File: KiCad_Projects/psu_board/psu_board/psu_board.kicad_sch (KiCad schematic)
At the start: 23 parts, among them J1 Conn_01x02_Female, J2 Conn_01x02_Female, J3 Conn_01x02_Female, SW1 SW_DIP_x01, SW2 SW_DIP_x01, SW3 SW_DIP_x01, SW4 SW_DIP_x01, SW5 SW_DIP_x01, U1 OKL-T_6-W12N-C

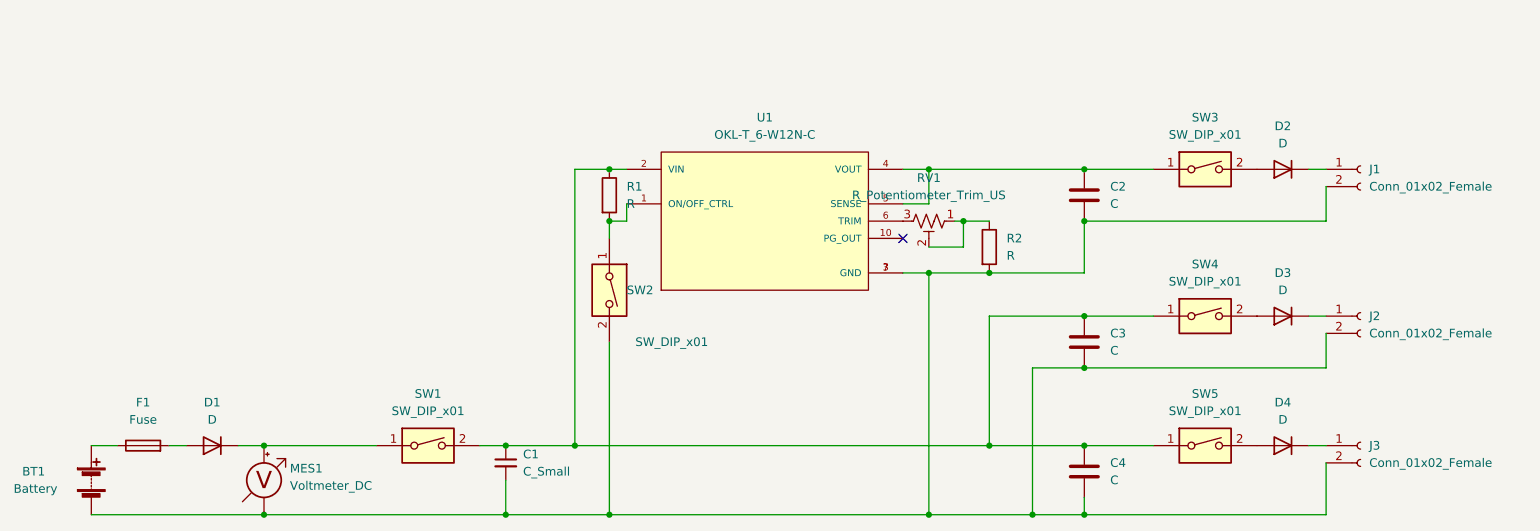
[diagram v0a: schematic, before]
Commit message: 基板データの更新
電源回路の更新、ライブラリの追加
やっと回路理解してきた！
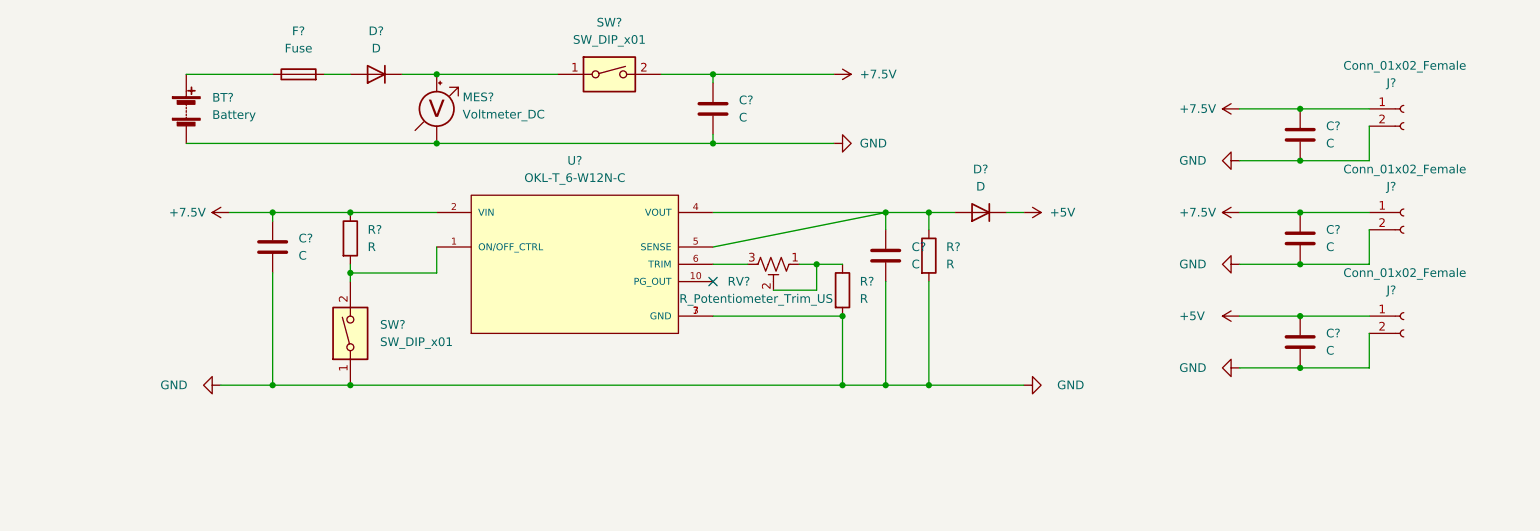
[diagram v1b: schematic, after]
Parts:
- removed BT1: Battery, symbol Device:Battery
- removed C1: C_Small, Capacitor_THT:C_Disc_D3.0mm_W1.6mm_P2.50mm, symbol Device:C_Small
- removed C2, C3, C4: C, Capacitor_THT:CP_Radial_D5.0mm_P2.50mm, symbol Device:C
- removed D1, D2, D3, D4: D, Diode_THT:D_A-405_P7.62mm_Horizontal, symbol Device:D
- removed F1: Fuse, symbol Device:Fuse
- removed J1, J2, J3: Conn_01x02_Female, Package_DIP:DIP-8-16_W7.62mm_Socket_LongPads, symbol Connector:Conn_01x02_Female
- removed MES1: Voltmeter_DC, Connector:SpringContact_Harwin_S1941-46R, symbol Device:Voltmeter_DC
- removed R1, R2: R, Resistor_THT:R_Axial_DIN0207_L6.3mm_D2.5mm_P7.62mm_Horizontal, symbol Device:R
- removed RV1: R_Potentiometer_Trim_US, symbol Device:R_Potentiometer_Trim_US
- removed SW1, SW2, SW3, SW4, SW5: SW_DIP_x01, symbol Switch:SW_DIP_x01
- removed U1: OKL-T_6-W12N-C, CONV_OKL-T_6-W12N-C, symbol OKL-T_6-W12N-C:OKL-T_6-W12N-C
- added BT?: Battery, symbol Device:Battery
- added C? (x6): C, symbol Device:C
- added D? (x2): D, symbol Device:D
- added F?: Fuse, symbol Device:Fuse
- added J? (x3): Conn_01x02_Female, symbol Connector:Conn_01x02_Female
- added MES?: Voltmeter_DC, symbol Device:Voltmeter_DC
- added R? (x3): R, symbol Device:R
- added RV?: R_Potentiometer_Trim_US, symbol Device:R_Potentiometer_Trim_US
- added SW? (x2): SW_DIP_x01, symbol Switch:SW_DIP_x01
- added U?: OKL-T_6-W12N-C, CONV_OKL-T/6-W12N-C, symbol OKL-T_6-W12N-C:OKL-T_6-W12N-C
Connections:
- new net: BT?.1 (+), F?.1
- new net: D?.2 (A), F?.2
- new net: C?.1, D?.2 (A), R?.1, U?.4 (VOUT), U?.5 (SENSE)
- new net: D?.1 (K), MES?.2 (+), SW?.1
- new net: R?.2, SW?.2, U?.1 (ON/OFF_CTRL)
- new net: R?.1, RV?.1, RV?.2
- new net: RV?.3, U?.6 (TRIM)
- new net +5V: C?.1, D?.1 (K), J?.1 (Pin_1)
- new net +7.5V: C?.1, C?.1, C?.1, C?.1, J?.1 (Pin_1), J?.1 (Pin_1), R?.1, SW?.2, U?.2 (VIN)
- new net GND: BT?.2 (-), C?.2, C?.2, C?.2, C?.2, C?.2, C?.2, J?.2 (Pin_2), J?.2 (Pin_2), J?.2 (Pin_2), MES?.1 (-), R?.2, R?.2, SW?.1, U?.3 (GND), U?.7 (GND)

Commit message: 基板データの更新
電源基盤の更新、フットプリントの割り当て中
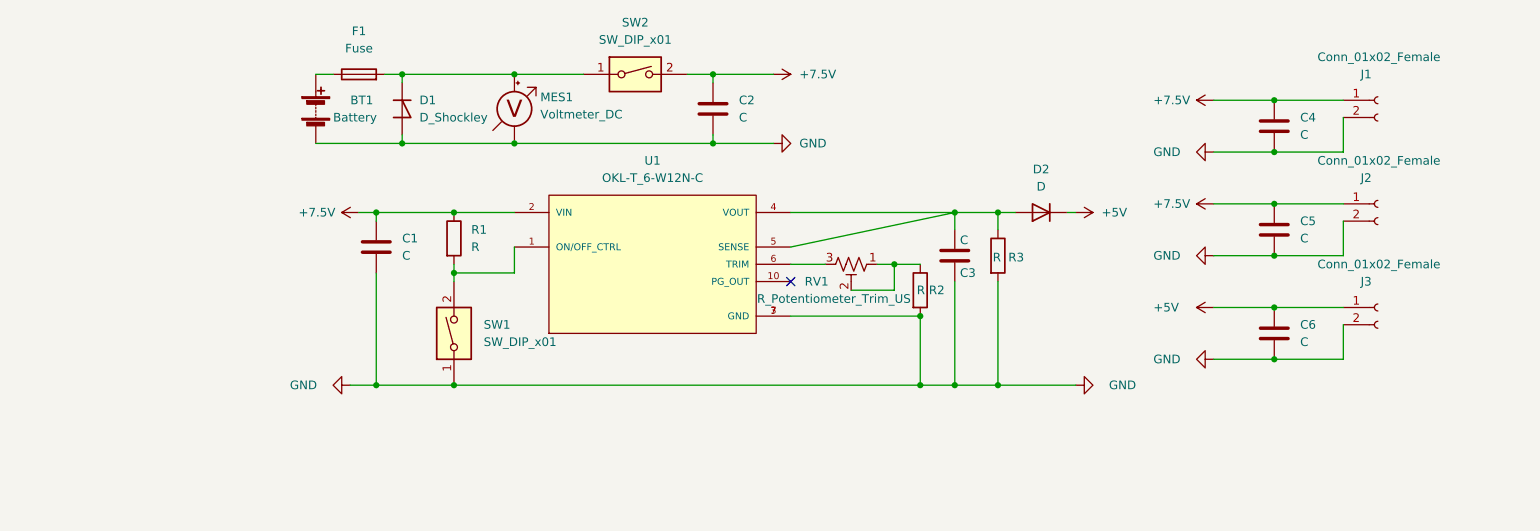
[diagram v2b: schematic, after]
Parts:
- removed D?: D, symbol Device:D
- added D1: D_Shockley, Diode_THT:D_5W_P10.16mm_Horizontal, symbol Device:D_Shockley
- C1, C3: renamed from C?; footprint (none) -> Capacitor_THT:C_Disc_D3.8mm_W2.6mm_P2.50mm
- C2, C4, C5, C6: renamed from C?; footprint (none) -> Capacitor_THT:CP_Radial_D5.0mm_P2.50mm
- D2: renamed from D?; footprint (none) -> Diode_THT:D_DO-41_SOD81_P7.62mm_Horizontal
- F1: renamed from F?; footprint (none) -> Fuse:Fuseholder_Keystone_3555-2
- U1: renamed from U?; footprint CONV_OKL-T/6-W12N-C -> CONV_OKL-T_6-W12N-C
- gave numbers to parts that had none: 11
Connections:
- net GND: now also D1.2 (A)
- net at F1.2: now also MES1.2 (+), SW2.1, D1.1 (K)
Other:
- moved on the sheet: BT1, C1, C3, C4, C5, C6, D2, F1, J1, J2, J3, MES1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

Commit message: 基盤データの更新　
電源基盤のフットプリントの割り当て完了
配線開始。
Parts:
- F1: footprint Fuse:Fuseholder_Keystone_3555-2 -> (none)
- U1: footprint CONV_OKL-T_6-W12N-C -> (none)
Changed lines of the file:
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@@
     (property "Reference" "F1" (id 0) (at 86.36 69.85 90))
     (property "Value" "Fuse" (id 1) (at 86.36 72.39 90))
-    (property "Footprint" "Fuse:Fuseholder_Keystone_3555-2" (id 2) (at 86.36 77.978 90)
+    (property "Footprint" "" (id 2) (at 86.36 77.978 90)
       (effects (font (size 1.27 1.27)) hide)
     )
@@
     (property "Reference" "U1" (id 0) (at 129.54 88.9 0))
     (property "Value" "OKL-T_6-W12N-C" (id 1) (at 129.54 91.44 0))
-    (property "Footprint" "CONV_OKL-T_6-W12N-C" (id 2) (at 118.11 92.71 0)
+    (property "Footprint" "" (id 2) (at 118.11 92.71 0)
       (effects (font (size 1.27 1.27)) (justify left bottom) hide)
     )
@@
     )
     (path "/1225119b-c748-4267-a0ec-ece61974b0e3"
-      (reference "BT1") (unit 1) (value "Battery") (footprint "")
+      (reference "BT1") (unit 1) (value "Battery") (footprint "Connector_JST:JST_EH_B2B-EH-A_1x02_P2.50mm_Vertical")
     )
     (path "/d9f3e0d8-7d2b-4a9d-9ced-0ae75299485c"
@@
     )
     (path "/2197c9be-58d1-4c42-8c39-5759355f3cec"
-      (reference "F1") (unit 1) (value "Fuse") (footprint "Fuse:Fuseholder_Keystone_3555-2")
+      (reference "F1") (unit 1) (value "Fuse") (footprint "Lib:fuse_socket")
     )
     (path "/b5f584d8-e2f1-4466-bad5-fc454a16bd66"
-      (reference "J1") (unit 1) (value "Conn_01x02_Female") (footprint "")
+      (reference "J1") (unit 1) (value "Conn_01x02_Female") (footprint "Connector_PinSocket_2.54mm:PinSocket_1x02_P2.54mm_Vertical")
     )
     (path "/61f99c06-3bbf-4774-a9aa-1ba3fc75384a"
-      (reference "J2") (unit 1) (value "Conn_01x02_Female") (footprint "")
+      (reference "J2") (unit 1) (value "Conn_01x02_Female") (footprint "Connector_PinSocket_2.54mm:PinSocket_1x02_P2.54mm_Vertical")
     )
     (path "/ff4b59d2-a393-4239-b5ac-d0c0f747c6f4"
-      (reference "J3") (unit 1) (value "Conn_01x02_Female") (footprint "")
+      (reference "J3") (unit 1) (value "Conn_01x02_Female") (footprint "Connector_PinSocket_2.54mm:PinSocket_1x02_P2.54mm_Vertical")
     )
     (path "/5699b960-e611-49fc-88b9-5b2baa2144b2"
-      (reference "MES1") (unit 1) (value "Voltmeter_DC") (footprint "")
+      (reference "MES1") (unit 1) (value "Voltmeter_DC") (footprint "Lib:voltage_counter")
     )
     (path "/cabf5c2a-03cd-4981-adc3-ed8179e7a3cf"
-      (reference "R1") (unit 1) (value "R") (footprint "")
+      (reference "R1") (unit 1) (value "R") (footprint "Resistor_THT:R_Axial_DIN0204_L3.6mm_D1.6mm_P5.08mm_Horizontal")
     )
     (path "/b2ad0b04-d548-41b9-b64b-32ecbc55afcf"
-      (reference "R2") (unit 1) (value "R") (footprint "")
+      (reference "R2") (unit 1) (value "R") (footprint "Resistor_THT:R_Axial_DIN0204_L3.6mm_D1.6mm_P5.08mm_Horizontal")
     )
     (path "/4df6e0f6-0be0-4ec6-9cf6-14d4a5dcfd8b"
-      (reference "R3") (unit 1) (value "R") (footprint "")
+      (reference "R3") (unit 1) (value "R") (footprint "Resistor_THT:R_Axial_DIN0204_L3.6mm_D1.6mm_P5.08mm_Horizontal")
     )
     (path "/b6edc29d-70fe-4228-af35-e92092307519"
-      (reference "RV1") (unit 1) (value "R_Potentiometer_Trim_US") (footprint "")
+      (reference "RV1") (unit 1) (value "R_Potentiometer_Trim_US") (footprint "Potentiometer_THT:Potentiometer_Bourns_3296W_Vertical")
     )
     (path "/9a578099-0604-41cb-a4d9-8a3416290072"
-      (reference "SW1") (unit 1) (value "SW_DIP_x01") (footprint "")
+      (reference "SW1") (unit 1) (value "SW_DIP_x01") (footprint "Lib:2MS1T2B4M2QES")
     )
     (path "/5a582268-29ed-44ce-9390-9e20ec9ca330"
-      (reference "SW2") (unit 1) (value "SW_DIP_x01") (footprint "")
+      (reference "SW2") (unit 1) (value "SW_DIP_x01") (footprint "Lib:2MS1T2B4M2QES")
     )
     (path "/cd410f59-c42e-4444-b1f7-75876f2dc297"
-      (reference "U1") (unit 1) (value "OKL-T_6-W12N-C") (footprint "CONV_OKL-T_6-W12N-C")
-    )
-  )
+      (reference "U1") (unit 1) (value "OKL-T_6-W12N-C") (footprint "Lib:DCDC-murata-6A")
+    )
+  )

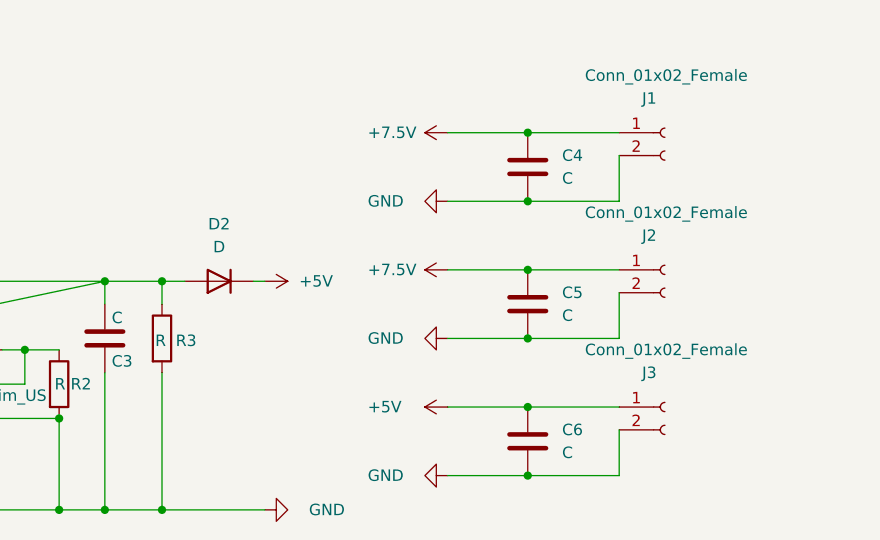
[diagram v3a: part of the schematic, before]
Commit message: 基盤データの更新
フットプリントの更新、電源基盤の部品の配置
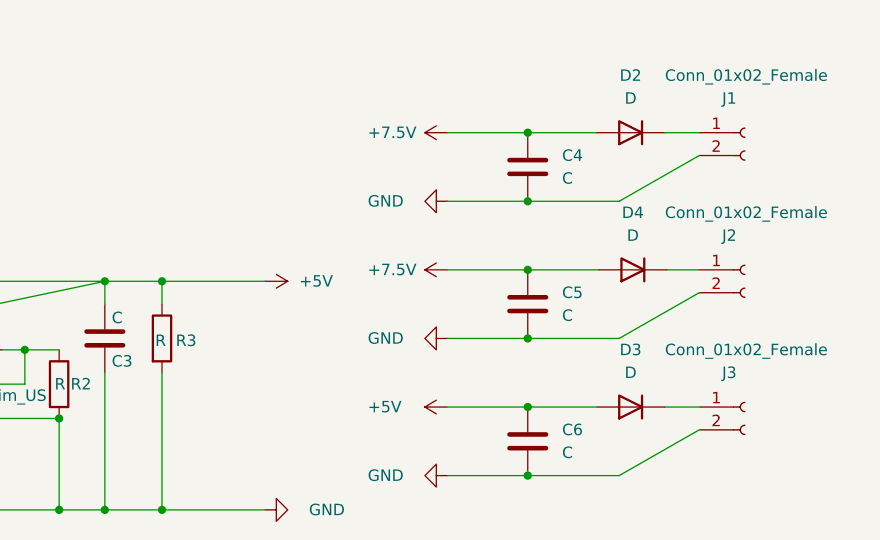
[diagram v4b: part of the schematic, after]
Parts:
- added D3, D4: D, Diode_THT:D_DO-41_SOD81_P7.62mm_Horizontal, symbol Device:D
- F1: footprint (none) -> Lib:fuse_socket
- J1, J2, J3: footprint (none) -> Connector_PinSocket_2.54mm:PinSocket_1x02_P2.54mm_Vertical
- MES1: footprint (none) -> Lib:voltage_counter
- R1, R2, R3: footprint (none) -> Resistor_THT:R_Axial_DIN0204_L3.6mm_D1.6mm_P5.08mm_Horizontal
- RV1: footprint (none) -> Potentiometer_THT:Potentiometer_Bourns_3296W_Vertical
- SW1: footprint (none) -> Lib:2MS1T2B4M2QES
- SW2: footprint (none) -> Lib:DS-850k
- U1: footprint (none) -> Lib:DCDC-murata-6A
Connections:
- net +5V: now also C3.1, R3.1, U1.4 (VOUT), U1.5 (SENSE), D3.2 (A); no longer D2.1 (K), J3.1 (Pin_1)
- net +7.5V: now also D2.2 (A), D4.2 (A); no longer J1.1 (Pin_1), J2.1 (Pin_1)
- new net: D2.1 (K), J1.1 (Pin_1)
- new net: D4.1 (K), J2.1 (Pin_1)
- new net: D3.1 (K), J3.1 (Pin_1)
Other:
- moved on the sheet: J1, J2, J3
